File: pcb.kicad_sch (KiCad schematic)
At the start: 13 parts

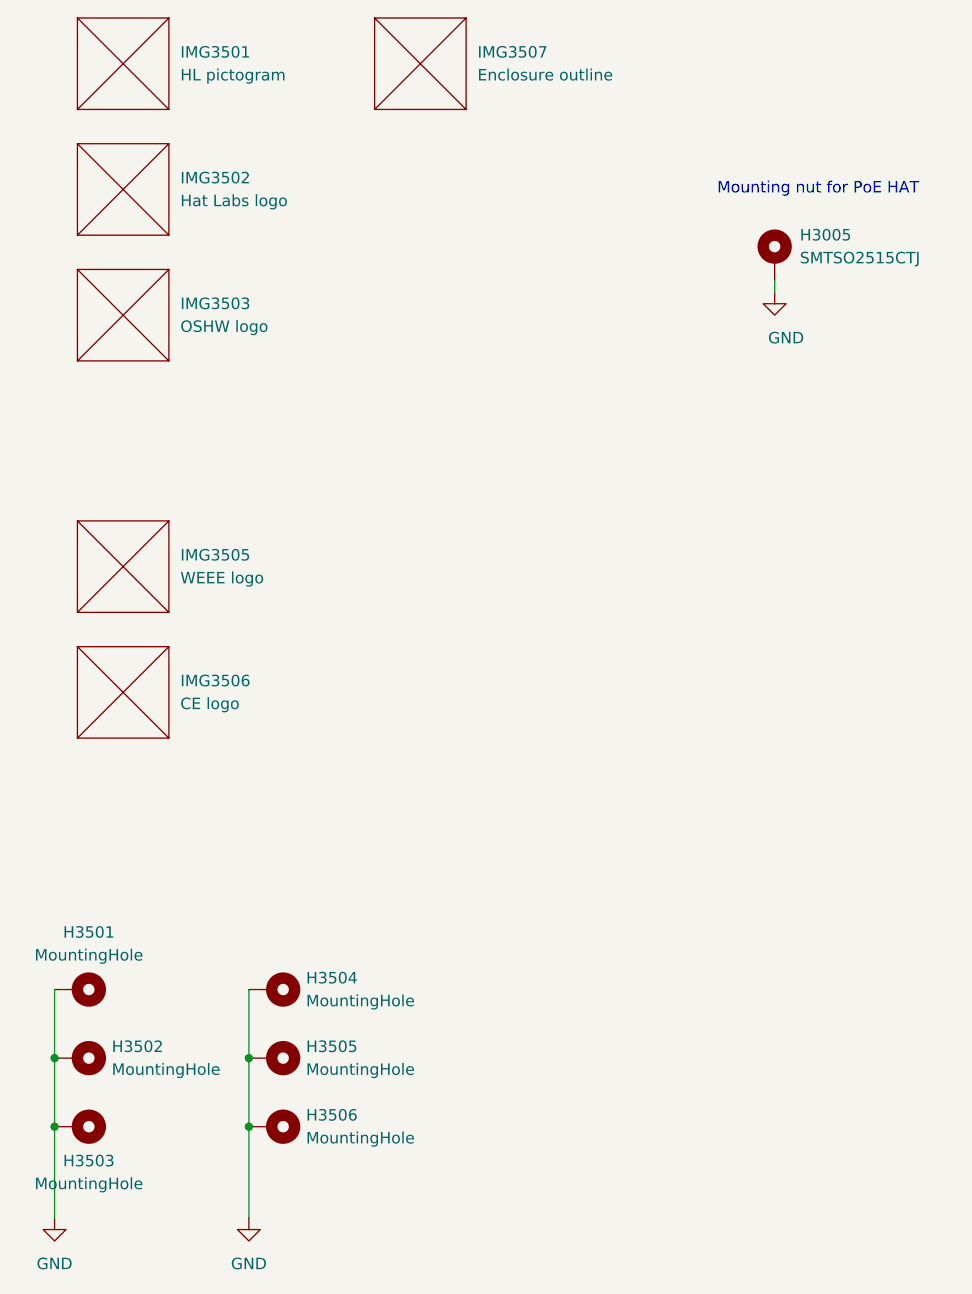
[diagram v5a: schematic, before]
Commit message: Finish the board redesign with SoM on the bottom
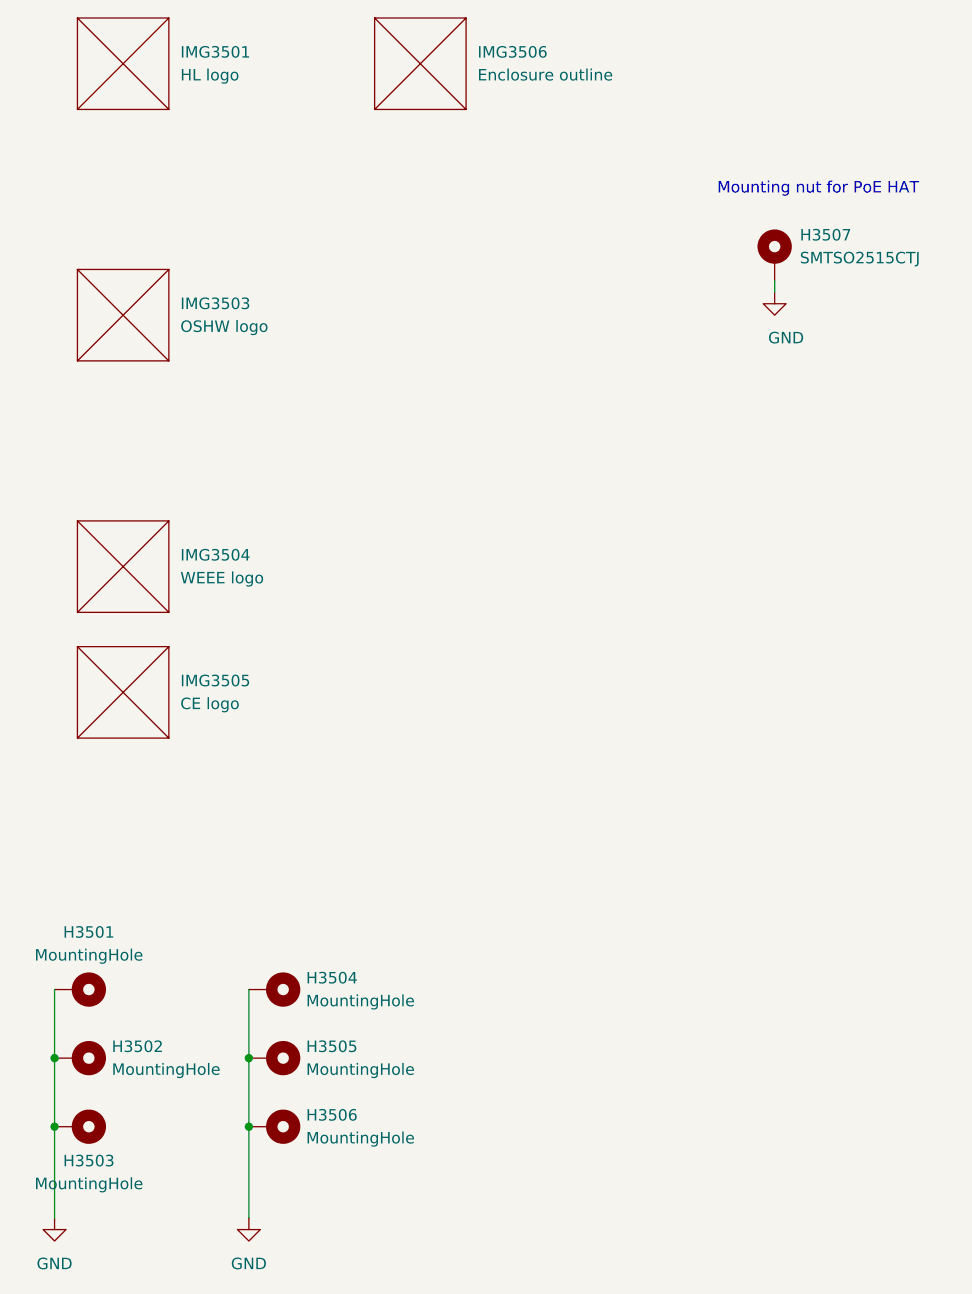
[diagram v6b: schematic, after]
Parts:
- removed IMG3502: Hat Labs logo, Hatlabs:Hat_Labs_13mm, symbol Hatlabs:SilkScreenImage
- IMG3501: value HL pictogram -> HL logo; footprint Hatlabs:HL_picto_halftone_70mm -> Hatlabs:Hat_Labs_logo_20mm
- renumbered H3005 to H3507, IMG3505 to IMG3504, IMG3506 to IMG3505, IMG3507 to IMG3506
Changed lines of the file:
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@@
 		(dnp no)
 		(fields_autoplaced yes)
-		(property "Reference" "IMG3505"
+		(property "Reference" "IMG3504"
 			(at 52.07 92.7099 0)
 			(effects
@@
 			(project "HALPI2"
 				(path "/abc482bd-3f17-4d35-80db-1da3dcdb5c27/e4643111-53ad-48d1-8ad1-a500e184f609"
-					(reference "IMG3505")
-					(unit 1)
-				)
-			)
-		)
-	)
-	(symbol
-		(lib_name "MountingHole_Pad_1")
+					(reference "IMG3504")
+					(unit 1)
+				)
+			)
+		)
+	)
+	(symbol
 		(lib_id "Mechanical:MountingHole_Pad")
 		(at 62.23 156.21 270)
@@
 	(symbol
 		(lib_id "Hatlabs:SilkScreenImage")
-		(at 45.72 49.53 0)
-		(unit 1)
-		(exclude_from_sim no)
-		(in_bom no)
-		(on_board yes)
-		(dnp no)
-		(fields_autoplaced yes)
-		(property "Reference" "IMG3502"
-			(at 52.07 50.7999 0)
-			(effects
-				(font
-					(size 1.27 1.27)
-				)
-				(justify left)
-			)
-		)
-		(property "Value" "Hat Labs logo"
-			(at 52.07 53.3399 0)
-			(effects
-				(font
-					(size 1.27 1.27)
-				)
-				(justify left)
-			)
-		)
-		(property "Footprint" "Hatlabs:Hat_Labs_13mm"
-			(at 45.72 49.53 0)
-			(effects
-				(font
-					(size 1.27 1.27)
-				)
-				(hide yes)
-			)
-		)
-		(property "Datasheet" ""
-			(at 45.72 49.53 0)
-			(effects
-				(font
-					(size 1.27 1.27)
-				)
-				(hide yes)
-			)
-		)
-		(property "Description" ""
-			(at 45.72 49.53 0)
-			(effects
-				(font
-					(size 1.27 1.27)
-				)
-				(hide yes)
-			)
-		)
-		(property "Characteristics" ""
-			(at 45.72 49.53 0)
-			(effects
-				(font
-					(size 1.27 1.27)
-				)
-				(hide yes)
-			)
-		)
-		(instances
-			(project "HALPI2"
-				(path "/abc482bd-3f17-4d35-80db-1da3dcdb5c27/e4643111-53ad-48d1-8ad1-a500e184f609"
-					(reference "IMG3502")
-					(unit 1)
-				)
-			)
-		)
-	)
-	(symbol
-		(lib_id "Hatlabs:SilkScreenImage")
 		(at 45.72 63.5 0)
 		(unit 1)
@@
 	)
 	(symbol
-		(lib_name "MountingHole_Pad_2")
 		(lib_id "Mechanical:MountingHole_Pad")
 		(at 62.23 140.97 270)
@@
 	)
 	(symbol
-		(lib_name "MountingHole_Pad_3")
 		(lib_id "Mechanical:MountingHole_Pad")
 		(at 62.23 148.59 270)
@@
 		(on_board yes)
 		(dnp no)
-		(property "Reference" "#PWR03009"
+		(property "Reference" "#PWR03503"
 			(at 118.11 69.85 0)
 			(effects
@@
 			(project "HALPI2"
 				(path "/abc482bd-3f17-4d35-80db-1da3dcdb5c27/e4643111-53ad-48d1-8ad1-a500e184f609"
-					(reference "#PWR03009")
-					(unit 1)
-				)
-			)
-		)
-	)
-	(symbol
-		(lib_name "MountingHole_Pad_4")
+					(reference "#PWR03503")
+					(unit 1)
+				)
+			)
+		)
+	)
+	(symbol
 		(lib_id "Mechanical:MountingHole_Pad")
 		(at 40.64 148.59 270)
@@
 		(dnp no)
 		(fields_autoplaced yes)
-		(property "Reference" "H3005"
+		(property "Reference" "H3507"
 			(at 120.904 57.1499 0)
 			(effects
@@
 			)
 		)
-		(property "Description" ""
+		(property "Description" "Mounting Hole with connection"
 			(at 118.11 59.69 0)
 			(effects
@@
 			(project "HALPI2"
 				(path "/abc482bd-3f17-4d35-80db-1da3dcdb5c27/e4643111-53ad-48d1-8ad1-a500e184f609"
-					(reference "H3005")
+					(reference "H3507")
 					(unit 1)
 				)
@@
 		(dnp no)
 		(fields_autoplaced yes)
-		(property "Reference" "IMG3507"
+		(property "Reference" "IMG3506"
 			(at 85.09 36.8299 0)
 			(effects
@@
 			(project "HALPI2"
 				(path "/abc482bd-3f17-4d35-80db-1da3dcdb5c27/e4643111-53ad-48d1-8ad1-a500e184f609"
-					(reference "IMG3507")
-					(unit 1)
-				)
-			)
-		)
-	)
-	(symbol
-		(lib_name "MountingHole_Pad_5")
+					(reference "IMG3506")
+					(unit 1)
+				)
+			)
+		)
+	)
+	(symbol
 		(lib_id "Mechanical:MountingHole_Pad")
 		(at 40.64 140.97 270)
@@
 			)
 		)
-		(property "Value" "HL pictogram"
+		(property "Value" "HL logo"
 			(at 52.07 39.3699 0)
 			(effects
@@
 			)
 		)
-		(property "Footprint" "Hatlabs:HL_picto_halftone_70mm"
+		(property "Footprint" "Hatlabs:Hat_Labs_logo_20mm"
 			(at 45.72 35.56 0)
 			(effects
@@
 	)
 	(symbol
-		(lib_name "MountingHole_Pad_6")
 		(lib_id "Mechanical:MountingHole_Pad")
 		(at 40.64 156.21 270)
@@
 		(dnp no)
 		(fields_autoplaced yes)
-		(property "Reference" "IMG3506"
+		(property "Reference" "IMG3505"
 			(at 52.07 106.6799 0)
 			(effects
@@
 			(project "HALPI2"
 				(path "/abc482bd-3f17-4d35-80db-1da3dcdb5c27/e4643111-53ad-48d1-8ad1-a500e184f609"
-					(reference "IMG3506")
-					(unit 1)
-				)
+					(reference "IMG3505")
+					(unit 1)
+				)

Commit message: Further refinements
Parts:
- H3501, H3502, H3503, H3504, H3505, H3506: footprint MountingHole:MountingHole_2.2mm_M2_Pad_Via -> MountingHole:MountingHole_4.3mm_M4_Pad_Via
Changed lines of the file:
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@@
+			)
+		)
+		(property "LCSC Part" ""
+			(at 45.72 91.44 0)
+			(effects
+				(font
+					(size 1.27 1.27)
+				)
+			)
+		)
+		(property "Sim.Enable" ""
+			(at 45.72 91.44 0)
+			(effects
+				(font
+					(size 1.27 1.27)
+				)
 			)
 		)
@@
 			)
 		)
-		(property "Footprint" "MountingHole:MountingHole_2.2mm_M2_Pad_Via"
+		(property "Footprint" "MountingHole:MountingHole_4.3mm_M4_Pad_Via"
 			(at 62.23 156.21 0)
 			(effects
@@
 			)
 		)
+		(property "LCSC Part" ""
+			(at 62.23 156.21 0)
+			(effects
+				(font
+					(size 1.27 1.27)
+				)
+			)
+		)
+		(property "Sim.Enable" ""
+			(at 62.23 156.21 0)
+			(effects
+				(font
+					(size 1.27 1.27)
+				)
+			)
+		)
 		(pin "1"
 		)
@@
 			)
 		)
+		(property "LCSC Part" ""
+			(at 45.72 63.5 0)
+			(effects
+				(font
+					(size 1.27 1.27)
+				)
+			)
+		)
+		(property "Sim.Enable" ""
+			(at 45.72 63.5 0)
+			(effects
+				(font
+					(size 1.27 1.27)
+				)
+			)
+		)
 		(instances
 			(project "HALPI2"
@@
 			)
 		)
-		(property "Footprint" "MountingHole:MountingHole_2.2mm_M2_Pad_Via"
+		(property "Footprint" "MountingHole:MountingHole_4.3mm_M4_Pad_Via"
 			(at 62.23 140.97 0)
 			(effects
@@
 			)
 		)
+		(property "LCSC Part" ""
+			(at 62.23 140.97 0)
+			(effects
+				(font
+					(size 1.27 1.27)
+				)
+			)
+		)
+		(property "Sim.Enable" ""
+			(at 62.23 140.97 0)
+			(effects
+				(font
+					(size 1.27 1.27)
+				)
+			)
+		)
 		(pin "1"
 		)
@@
 			)
 		)
-		(property "Footprint" "MountingHole:MountingHole_2.2mm_M2_Pad_Via"
+		(property "Footprint" "MountingHole:MountingHole_4.3mm_M4_Pad_Via"
 			(at 62.23 148.59 0)
 			(effects
@@
 			)
 		)
+		(property "LCSC Part" ""
+			(at 62.23 148.59 0)
+			(effects
+				(font
+					(size 1.27 1.27)
+				)
+			)
+		)
+		(property "Sim.Enable" ""
+			(at 62.23 148.59 0)
+			(effects
+				(font
+					(size 1.27 1.27)
+				)
+			)
+		)
 		(pin "1"
 		)
@@
 			)
 		)
-		(property "Footprint" "MountingHole:MountingHole_2.2mm_M2_Pad_Via"
+		(property "Footprint" "MountingHole:MountingHole_4.3mm_M4_Pad_Via"
 			(at 40.64 148.59 0)
 			(effects
@@
 			)
 		)
+		(property "LCSC Part" ""
+			(at 40.64 148.59 0)
+			(effects
+				(font
+					(size 1.27 1.27)
+				)
+			)
+		)
+		(property "Sim.Enable" ""
+			(at 40.64 148.59 0)
+			(effects
+				(font
+					(size 1.27 1.27)
+				)
+			)
+		)
 		(pin "1"
 		)
@@
 			)
 		)
+		(property "LCSC Part" ""
+			(at 118.11 59.69 0)
+			(effects
+				(font
+					(size 1.27 1.27)
+				)
+			)
+		)
+		(property "Sim.Enable" ""
+			(at 118.11 59.69 0)
+			(effects
+				(font
+					(size 1.27 1.27)
+				)
+			)
+		)
 		(pin "1"
 		)
@@
 			)
 		)
+		(property "LCSC Part" ""
+			(at 78.74 35.56 0)
+			(effects
+				(font
+					(size 1.27 1.27)
+				)
+			)
+		)
+		(property "Sim.Enable" ""
+			(at 78.74 35.56 0)
+			(effects
+				(font
+					(size 1.27 1.27)
+				)
+			)
+		)
 		(instances
 			(project "HALPI2"
@@
 			)
 		)
-		(property "Footprint" "MountingHole:MountingHole_2.2mm_M2_Pad_Via"
+		(property "Footprint" "MountingHole:MountingHole_4.3mm_M4_Pad_Via"
 			(at 40.64 140.97 0)
 			(effects
@@
 			)
 		)
+		(property "LCSC Part" ""
+			(at 40.64 140.97 0)
+			(effects
+				(font
+					(size 1.27 1.27)
+				)
+			)
+		)
+		(property "Sim.Enable" ""
+			(at 40.64 140.97 0)
+			(effects
+				(font
+					(size 1.27 1.27)
+				)
+			)
+		)
 		(pin "1"
 		)
@@
 			)
 		)
+		(property "LCSC Part" ""
+			(at 45.72 35.56 0)
+			(effects
+				(font
+					(size 1.27 1.27)
+				)
+			)
+		)
+		(property "Sim.Enable" ""
+			(at 45.72 35.56 0)
+			(effects
+				(font
+					(size 1.27 1.27)
+				)
+			)
+		)
 		(instances
 			(project "HALPI2"
@@
 			)
 		)
-		(property "Footprint" "MountingHole:MountingHole_2.2mm_M2_Pad_Via"
+		(property "Footprint" "MountingHole:MountingHole_4.3mm_M4_Pad_Via"
 			(at 40.64 156.21 0)
 			(effects
@@
 			)
 		)
+		(property "LCSC Part" ""
+			(at 40.64 156.21 0)
+			(effects
+				(font
+					(size 1.27 1.27)
+				)
+			)
+		)
+		(property "Sim.Enable" ""
+			(at 40.64 156.21 0)
+			(effects
+				(font
+					(size 1.27 1.27)
+				)
+			)
+		)
 		(pin "1"
 		)
@@
 			)
 		)
+		(property "LCSC Part" ""
+			(at 45.72 105.41 0)
+			(effects
+				(font
+					(size 1.27 1.27)
+				)
+			)
+		)
+		(property "Sim.Enable" ""
+			(at 45.72 105.41 0)
+			(effects
+				(font
+					(size 1.27 1.27)
+				)
+			)
+		)

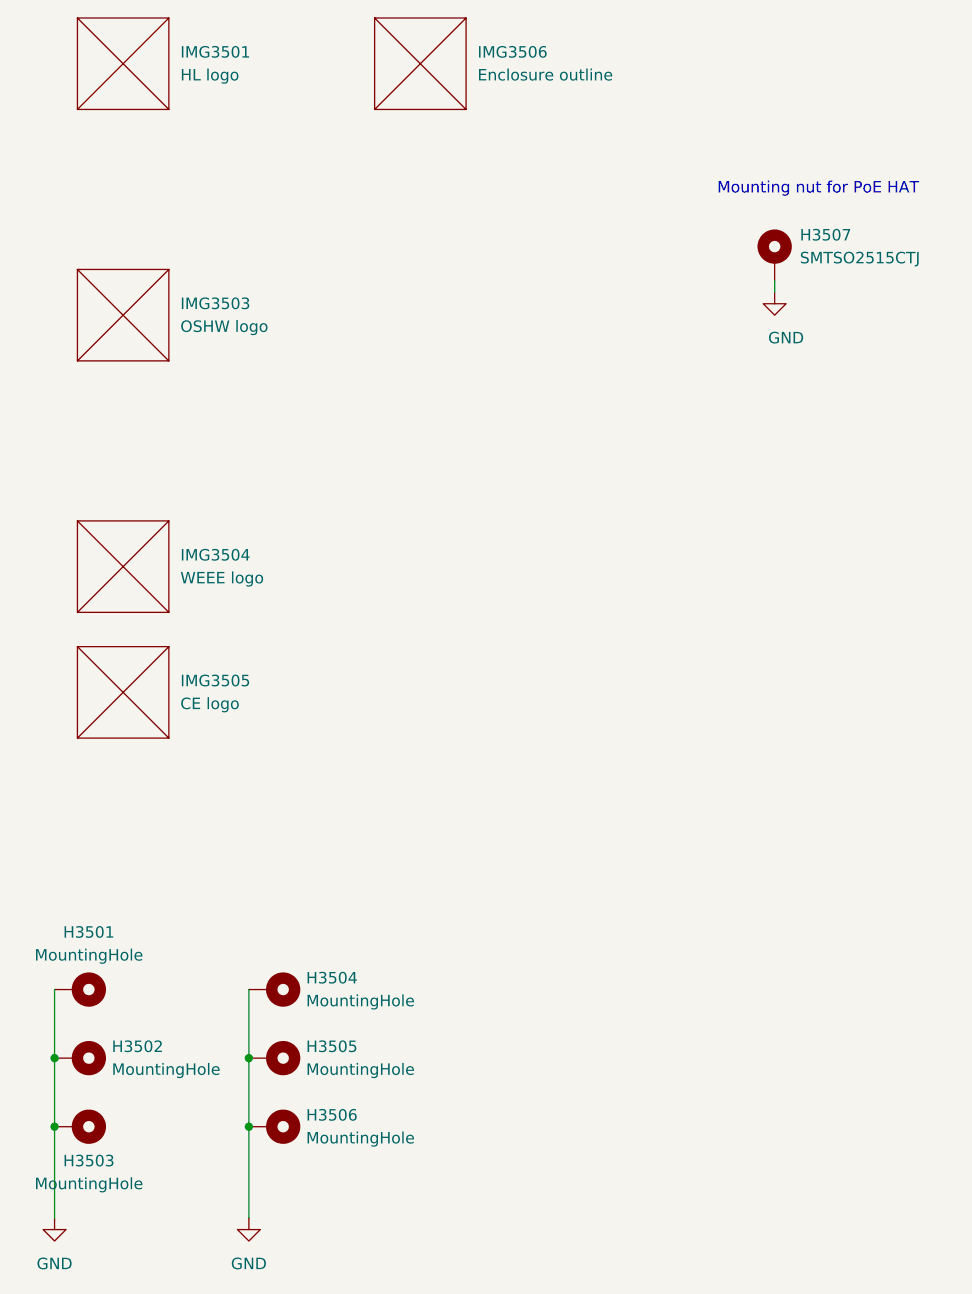
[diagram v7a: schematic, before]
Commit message: Finish transitioning to RP2040
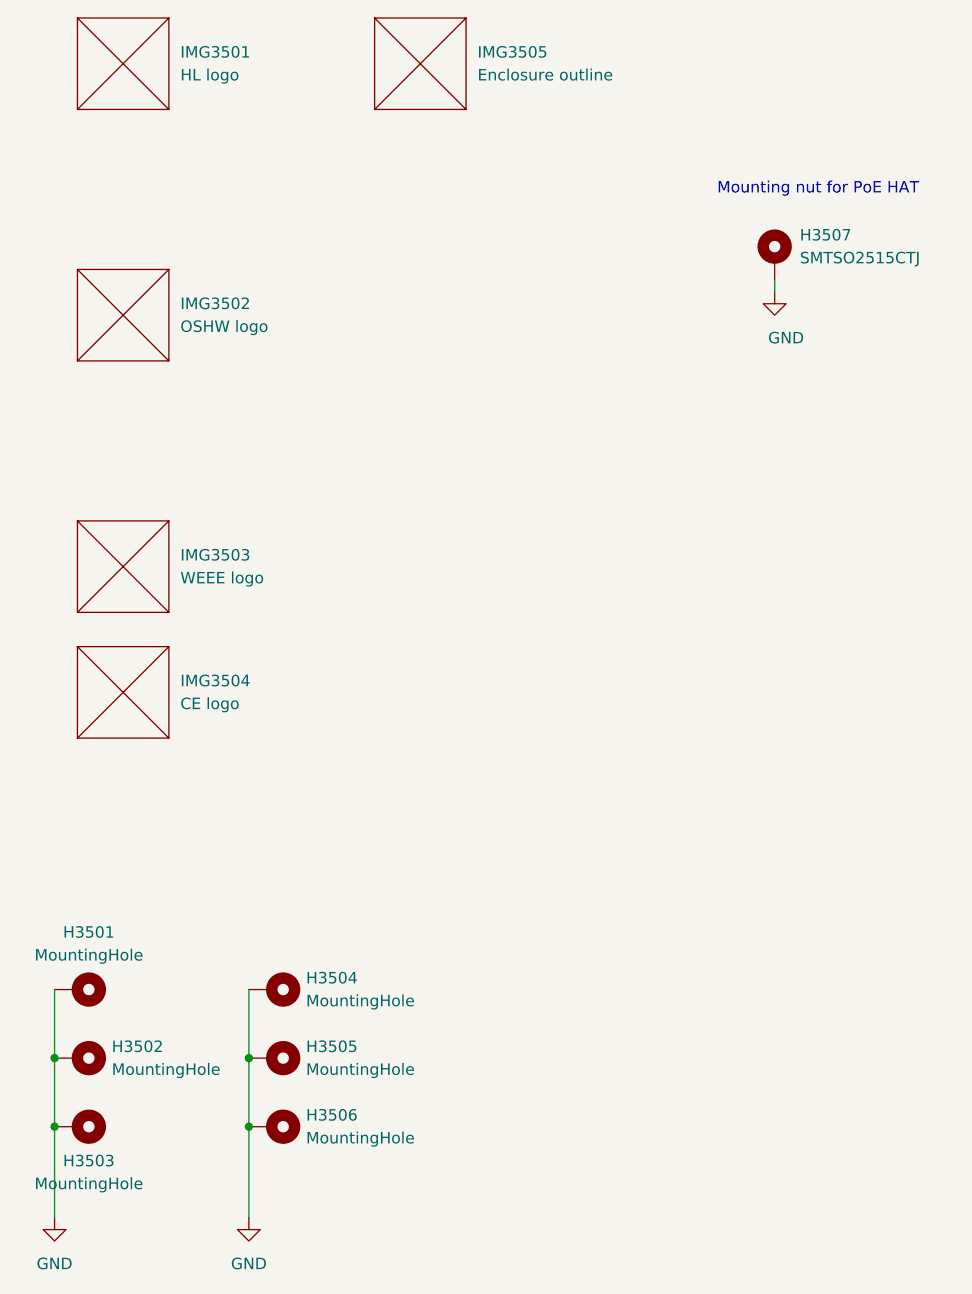
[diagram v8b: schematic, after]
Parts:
- renumbered IMG3503 to IMG3502, IMG3504 to IMG3503, IMG3505 to IMG3504, IMG3506 to IMG3505
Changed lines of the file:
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@@
 		(dnp no)
 		(fields_autoplaced yes)
-		(property "Reference" "IMG3504"
+		(property "Reference" "IMG3503"
 			(at 52.07 92.7099 0)
 			(effects
@@
 			(project "HALPI2"
 				(path "/abc482bd-3f17-4d35-80db-1da3dcdb5c27/e4643111-53ad-48d1-8ad1-a500e184f609"
-					(reference "IMG3504")
+					(reference "IMG3503")
 					(unit 1)
 				)
@@
 		(dnp no)
 		(fields_autoplaced yes)
-		(property "Reference" "IMG3503"
+		(property "Reference" "IMG3502"
 			(at 52.07 64.7699 0)
 			(effects
@@
 			(project "HALPI2"
 				(path "/abc482bd-3f17-4d35-80db-1da3dcdb5c27/e4643111-53ad-48d1-8ad1-a500e184f609"
-					(reference "IMG3503")
+					(reference "IMG3502")
 					(unit 1)
 				)
@@
 		(dnp no)
 		(fields_autoplaced yes)
-		(property "Reference" "IMG3506"
+		(property "Reference" "IMG3505"
 			(at 85.09 36.8299 0)
 			(effects
@@
 			(project "HALPI2"
 				(path "/abc482bd-3f17-4d35-80db-1da3dcdb5c27/e4643111-53ad-48d1-8ad1-a500e184f609"
-					(reference "IMG3506")
+					(reference "IMG3505")
 					(unit 1)
 				)
@@
 		(dnp no)
 		(fields_autoplaced yes)
-		(property "Reference" "IMG3505"
+		(property "Reference" "IMG3504"
 			(at 52.07 106.6799 0)
 			(effects
@@
 			(project "HALPI2"
 				(path "/abc482bd-3f17-4d35-80db-1da3dcdb5c27/e4643111-53ad-48d1-8ad1-a500e184f609"
-					(reference "IMG3505")
-					(unit 1)
-				)
+					(reference "IMG3504")
+					(unit 1)
+				)
